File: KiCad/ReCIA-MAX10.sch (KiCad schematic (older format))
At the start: 29 parts, among them J1 Conn_02x03_Odd_Even, U1 AMS1117-3.3, U2 SN74CBT16210, U3 SN74CBT16210, U4 10M02SCU169, U5 8520_DIP_SOCKET, X1 Oscillator_3.2x2.5mm-28.6363M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

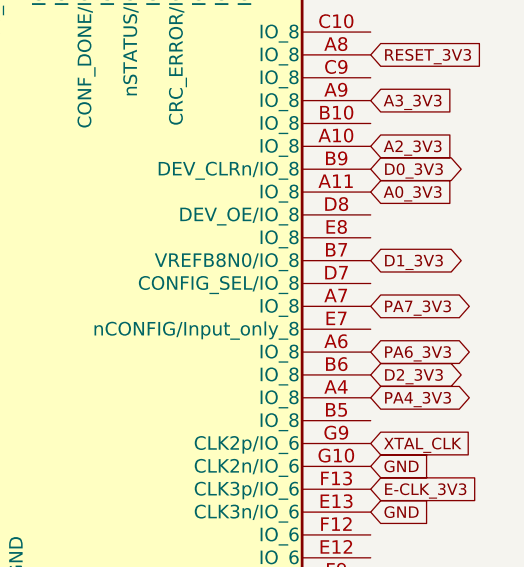
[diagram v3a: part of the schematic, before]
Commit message: Assign GND to CONFIG_SEL pad
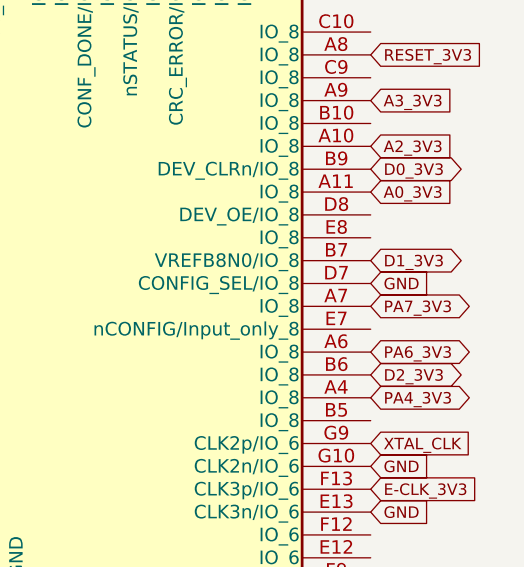
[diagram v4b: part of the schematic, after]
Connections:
- net GND: now also U4.D7 (CONFIG_SEL/IO_8)
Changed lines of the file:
@@
 Text Notes 2650 6800 0    50   ~ 0
 0603   0.01uF
+Text GLabel 10650 2750 2    50   Input ~ 0
+GND
 $EndSCHEMATC

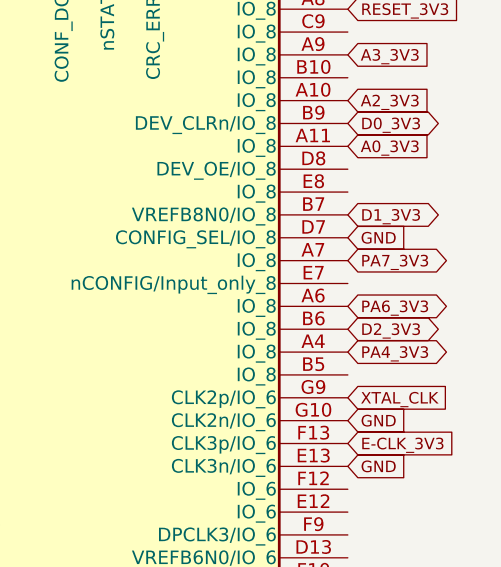
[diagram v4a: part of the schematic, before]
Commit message: Add nCONFIG signal
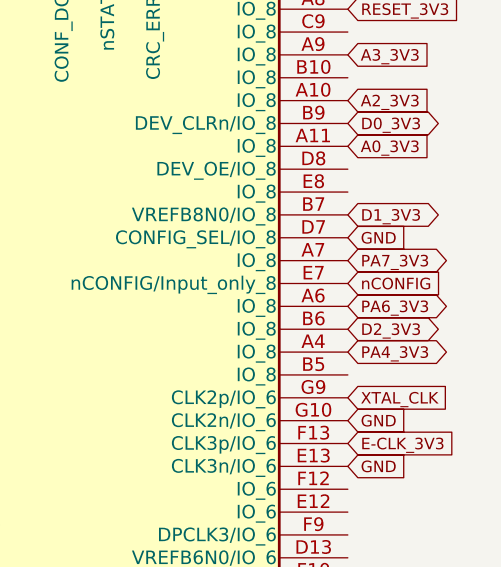
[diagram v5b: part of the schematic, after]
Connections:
- net nCONFIG: now reaches U4.E7 (nCONFIG/Input_only_8)
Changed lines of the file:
@@
 Text GLabel 10650 2750 2    50   Input ~ 0
 GND
+Text GLabel 10650 2950 2    50   Input ~ 0
+nCONFIG
 $EndSCHEMATC

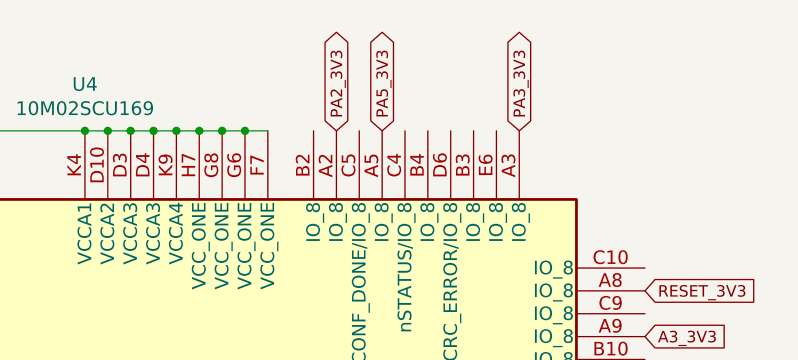
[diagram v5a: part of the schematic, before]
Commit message: Add nSTATUS signal
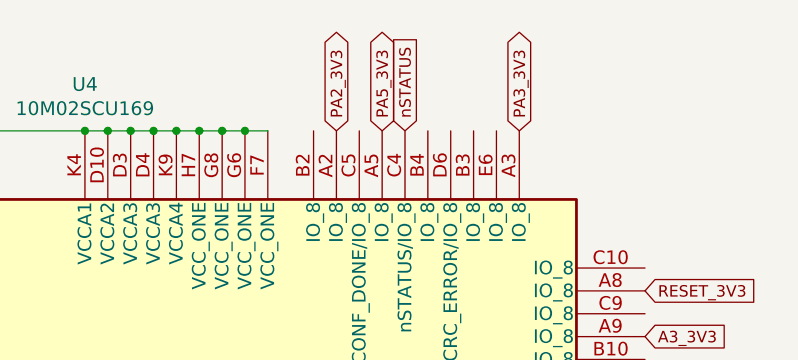
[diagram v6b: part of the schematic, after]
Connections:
- net nSTATUS: now reaches U4.C4 (nSTATUS/IO_8)
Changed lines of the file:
@@
 Text GLabel 10650 2950 2    50   Input ~ 0
 nCONFIG
+Text GLabel 9600 1050 1    50   Input ~ 0
+nSTATUS
 $EndSCHEMATC

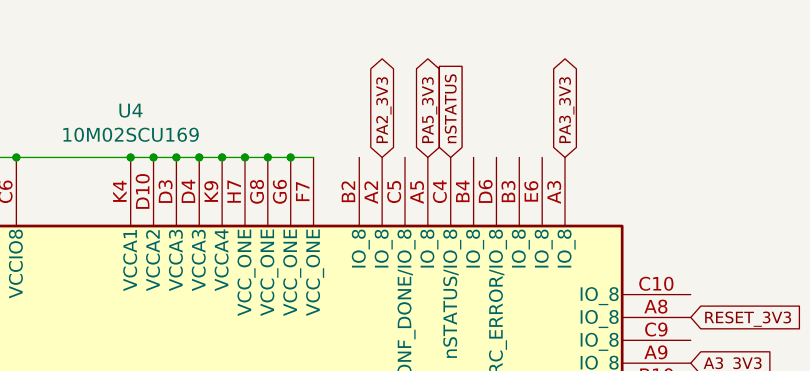
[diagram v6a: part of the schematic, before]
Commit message: Add CONF_DONE signal
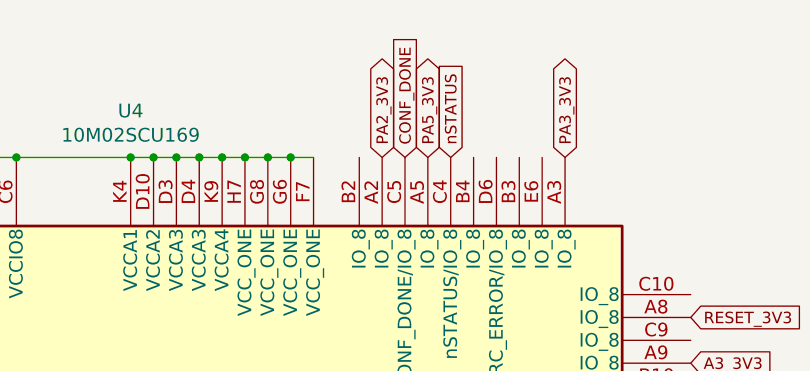
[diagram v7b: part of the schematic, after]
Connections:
- net CONF_DONE: now reaches U4.C5 (CONF_DONE/IO_8)
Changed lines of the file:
@@
 Text GLabel 9600 1050 1    50   Input ~ 0
 nSTATUS
+Text GLabel 9400 1050 1    50   Input ~ 0
+CONF_DONE
 $EndSCHEMATC

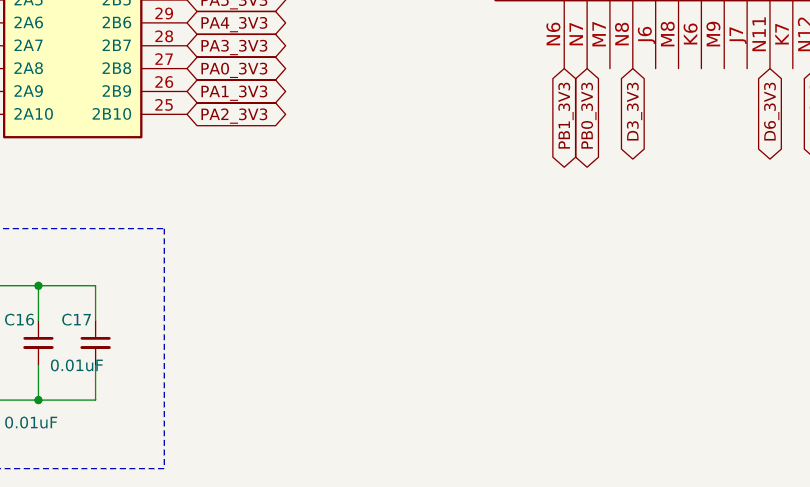
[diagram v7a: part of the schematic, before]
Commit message: Add 10k resistor pack RN1 and assign pull-ups for TMS, TDI and pull-down for TCK
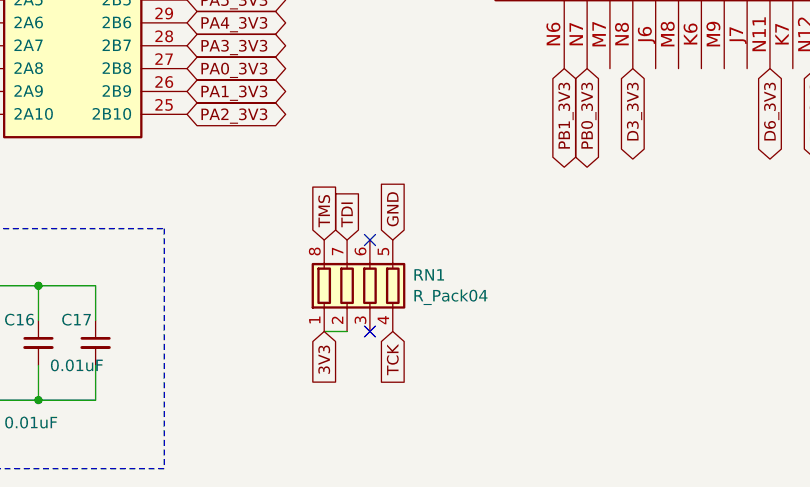
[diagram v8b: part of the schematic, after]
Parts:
- added RN1: R_Pack04, ReCIA:RESCAF80P320X160X60-8N, symbol Device:R_Pack04
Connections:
- net 3V3: now also RN1.1 (R1.1), RN1.2 (R2.1)
- net GND: now also RN1.5 (R4.2)
- net TCK: now also RN1.4 (R4.1)
- net TDI: now also RN1.7 (R2.2)
- net TMS: now also RN1.8 (R1.2)
- no-connect marks 2 -> 4
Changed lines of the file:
@@
 Text GLabel 9400 1050 1    50   Input ~ 0
 CONF_DONE
+$Comp
+L Device:R_Pack04 RN1
+U 1 1 672BF603
+P 5500 6900
+F 0 "RN1" H 5688 6946 50  0000 L CNN
+F 1 "R_Pack04" H 5688 6855 50  0000 L CNN
+F 2 "ReCIA:RESCAF80P320X160X60-8N" V 5775 6900 50  0001 C CNN
+F 3 "~" H 5500 6900 50  0001 C CNN
+	1    5500 6900
+	1    0    0    -1
+$EndComp
+Text GLabel 5600 6700 1    50   Input ~ 0
+GND
+Text GLabel 5600 7100 3    50   Input ~ 0
+TCK
+Text GLabel 5300 7100 3    50   Input ~ 0
+3V3
+Wire Wire Line
+	5300 7100 5400 7100
+Text GLabel 5300 6700 1    50   Input ~ 0
+TMS
+Text GLabel 5400 6700 1    50   Input ~ 0
+TDI
+NoConn ~ 5500 6700
+NoConn ~ 5500 7100
 $EndSCHEMATC
